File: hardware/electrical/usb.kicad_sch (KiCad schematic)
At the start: 0 parts

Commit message: Add USB PHY IC
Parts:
- added C29, C36, C37: 4u7, symbol Device:C_Small
- added C31, C32, C33, C34, C35: 100n, symbol Device:C_Small
- added C?: DNP, Capacitor_SMD:C_0402_1005Metric, symbol Device:C
- added D3: SMF6.0CA, symbol Device:D_TVS
- added FB?: 0R, Diode_SMD:D_0201_0603Metric, symbol Device:FerriteBead_Small
- added J1: USB_B_Micro, symbol Connector:USB_B_Micro
- added R10: 0R, symbol Device:R
- added R11: 12k±1%, symbol Device:R
- added U6: USB3300-EZK, Package_DFN_QFN:QFN-32-1EP_5x5mm_P0.5mm_EP3.45x3.45mm, symbol Interface_USB:USB3300-EZK
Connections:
- new net: C?.1, D3.2 (A2), FB?.1, J1.1 (VBUS)
- new net: C36.1, U6.29 (VDDA1.8)
- new net: R10.2, U6.4 (VBUS)
- new net: C37.1, U6.15 (VDD1.8), U6.26 (VDD1.8)
- new net: R11.1, U6.32 (RBIAS)
- new net +3V3: C29.1, C31.1, C32.1, C33.1, C34.1, C35.1, U6.16 (VDD3.3), U6.25 (VDD3.3), U6.30 (VDD3.3), U6.31 (REG_EN), U6.6 (VDD3.3)
- new net GND: C29.2, C31.2, C32.2, C33.2, C34.2, C35.2, C36.2, C37.2, C?.2, D3.1 (A1), J1.5 (GND), R11.2, U6.1 (GND), U6.2 (GND), U6.33 (GND)
- new net RCC_MCO_1: U6.28 (XI)
- new net USB_D+: J1.3 (D+), U6.7 (DP)
- new net USB_D-: J1.2 (D-), U6.8 (DM)
- new net USB_OTG_HS_RESET: U6.9 (RESET)
- new net USB_OTG_HS_ULPI_CLK: U6.14 (CLKOUT)
- new net USB_OTG_HS_ULPI_D0: U6.24 (DATA0)
- new net USB_OTG_HS_ULPI_D1: U6.23 (DATA1)
- new net USB_OTG_HS_ULPI_D2: U6.22 (DATA2)
- new net USB_OTG_HS_ULPI_D3: U6.21 (DATA3)
- new net USB_OTG_HS_ULPI_D4: U6.20 (DATA4)
- new net USB_OTG_HS_ULPI_D5: U6.19 (DATA5)
- new net USB_OTG_HS_ULPI_D6: U6.18 (DATA6)
- new net USB_OTG_HS_ULPI_D7: U6.17 (DATA7)
- new net USB_OTG_HS_ULPI_DIR: U6.12 (DIR)
- new net USB_OTG_HS_ULPI_NXT: U6.11 (NXT)
- new net USB_OTG_HS_ULPI_STP: U6.13 (STP)
- new net VBUS: FB?.2, R10.1
- no-connect marks 0 -> 6
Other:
- note added: "C30, C36 and C37 should all be low ESR (<1 Ohm)."
- note added: "NOTES"
- note added: "USB D- and D+ should be routed as a differential pair."
- note added: "USB3300 contains internal ESD protection."
- note added: "VBUS pin must never exceed 5.5V. D3 ensures voltage never exceeds 6V. R10 is available if necessary."
- company: (none) -> Frank Plowman
- title: (none) -> USB

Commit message: Update STM32CubeMX configuration to match schematic and fix ERC
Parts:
- gave numbers to parts that had none: 2
- renumbered C29 to C2, C31 to C3, C32 to C4, C33 to C5, C34 to C6, C35 to C7, C36 to C8, C37 to C9, D3 to D1, R10 to R1, R11 to R2, U6 to U1

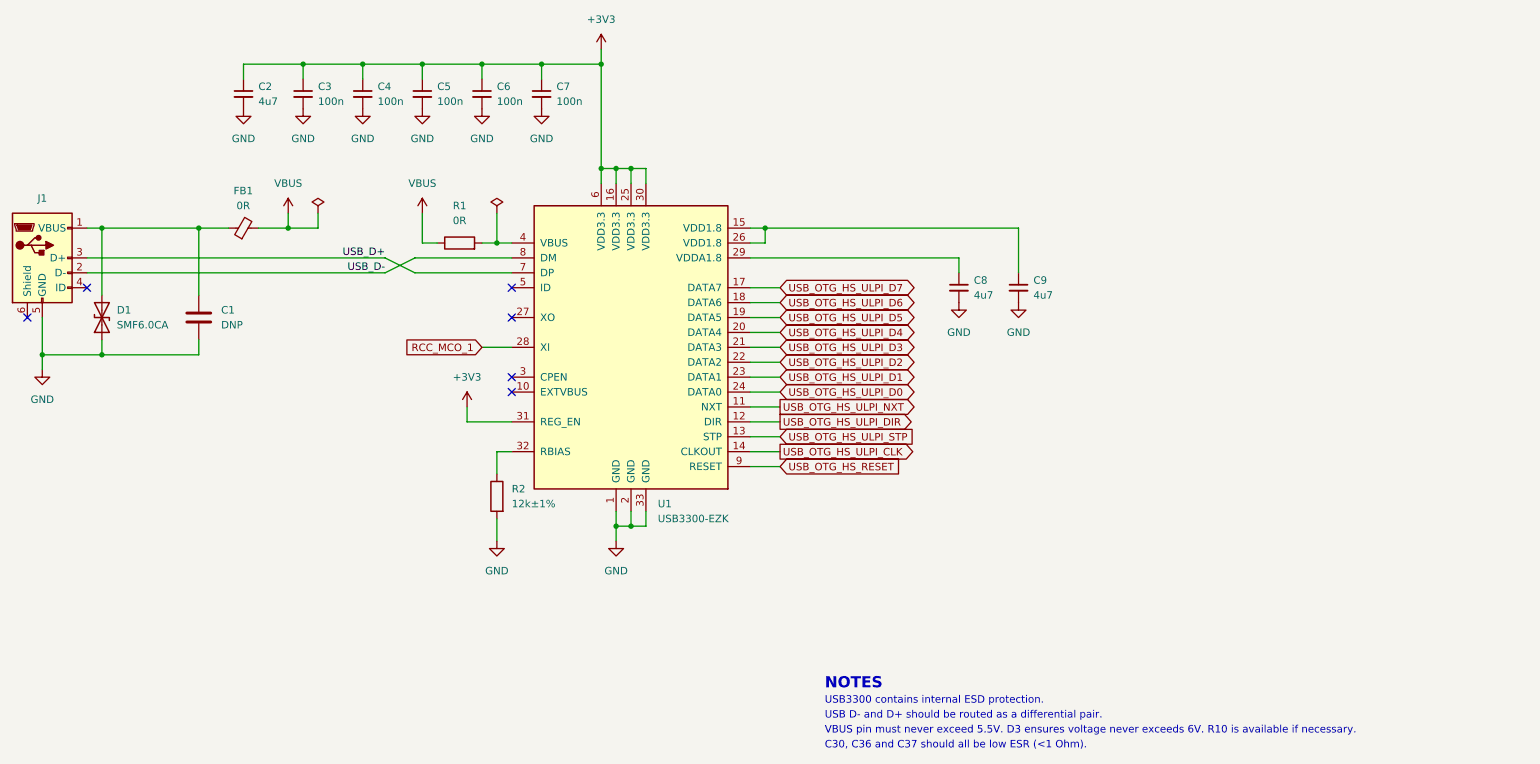
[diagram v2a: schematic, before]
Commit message: USB signal integrity tweaks. * Replace DNP capacitor at USB with 4.7µF per USB specification * Replace 0R ferrite bead with 100Ω@100MHz * Connect shield to ground * Replace 0R VBUS sense resistor with 670Ω to reject spikes 5.5V<V<6V * Add source terminator resistor for clock output
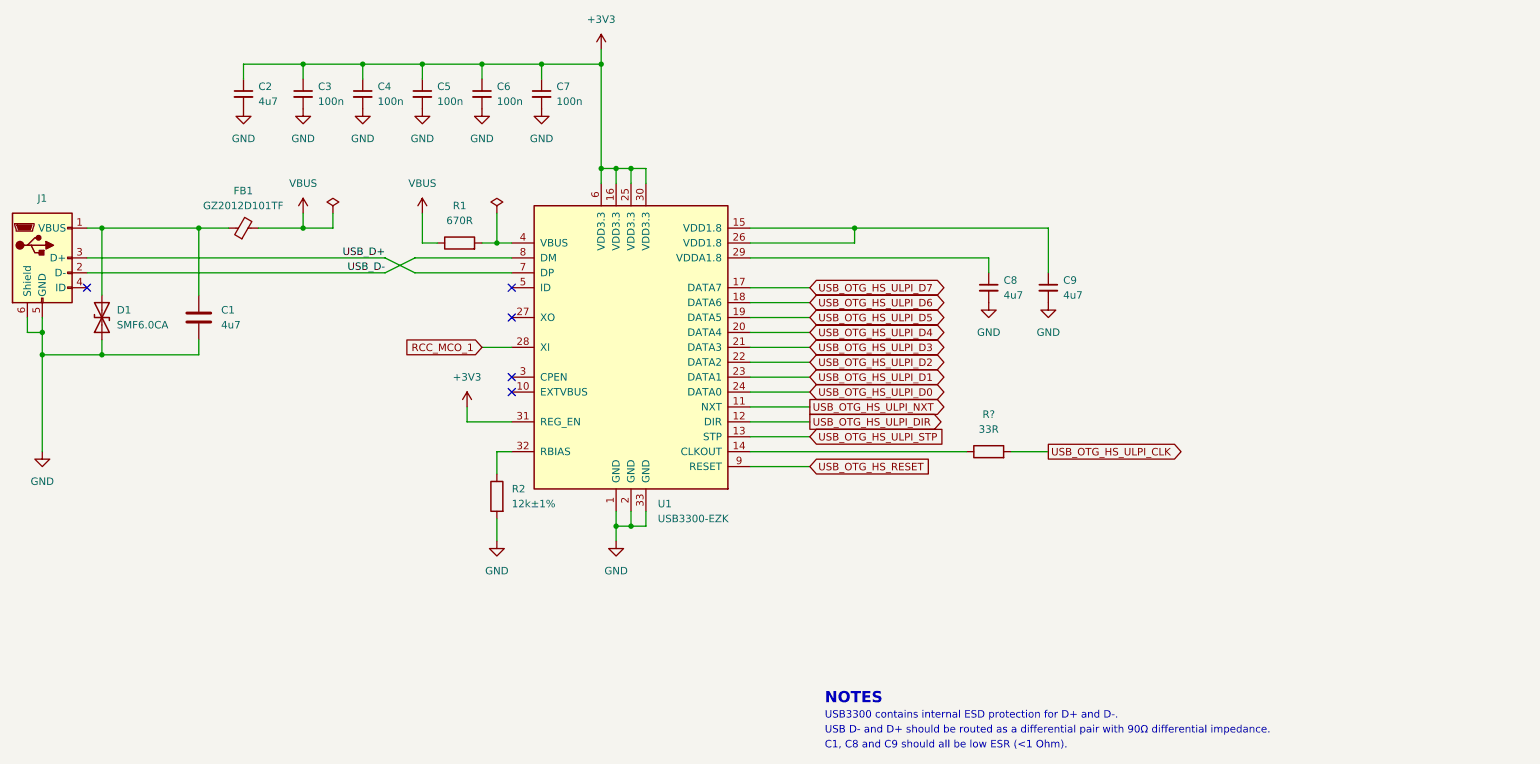
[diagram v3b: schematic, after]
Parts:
- added R?: 33R, symbol Device:R
- C1: value DNP -> 4u7
- FB1: value 0R -> GZ2012D101TF
- R1: value 0R -> 670R
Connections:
- net GND: now also J1.6 (Shield)
- net USB_OTG_HS_ULPI_CLK: now also R?.2; no longer U1.14 (CLKOUT)
- new net: R?.1, U1.14 (CLKOUT)
- no-connect marks 6 -> 5
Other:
- note added: "C1, C8 and C9 should all be low ESR (<1 Ohm)."
- note added: "USB D- and D+ should be routed as a differential pair with 90Ω differential impedance."
- note added: "USB3300 contains internal ESD protection for D+ and D-."
- note removed: "C30, C36 and C37 should all be low ESR (<1 Ohm)."
- note removed: "USB D- and D+ should be routed as a differential pair."
- note removed: "USB3300 contains internal ESD protection."
- note removed: "VBUS pin must never exceed 5.5V. D3 ensures voltage never exceeds 6V. R10 is available if necessary."
- moved on the sheet: C8, C9

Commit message: Minor USB schematic tweaks * Remove extra 100nF decoupling capacitor * Add notes on routing ULPI traces * Schematic formatting tweaks
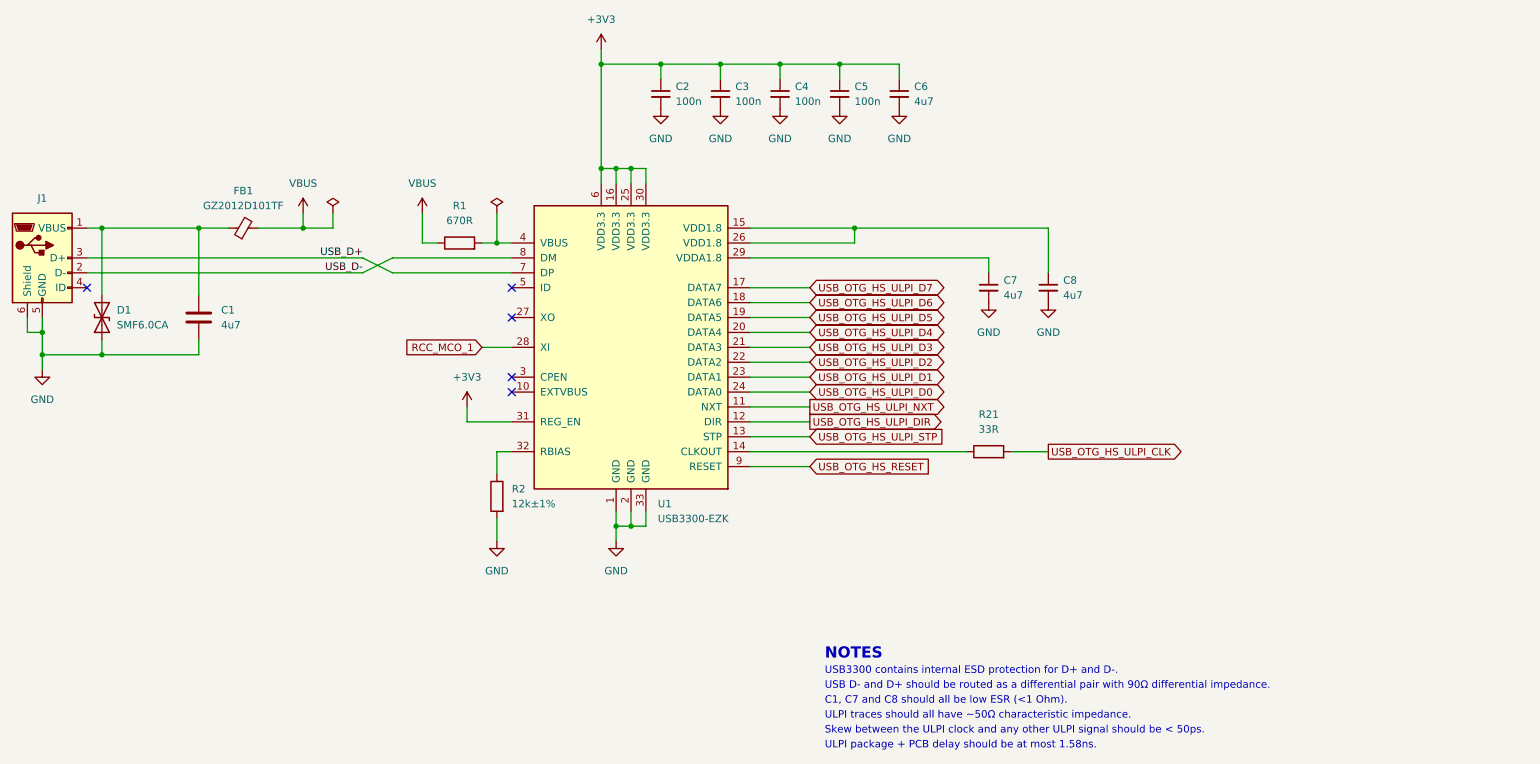
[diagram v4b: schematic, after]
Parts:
- removed C3: 100n, symbol Device:C_Small
- gave numbers to parts that had none: 1
- renumbered C7 to C2, C6 to C3, C5 to C4, C4 to C5, C2 to C6, C8 to C7, C9 to C8
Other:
- note added: "C1, C7 and C8 should all be low ESR (<1 Ohm)."
- note added: "Skew between the ULPI clock and any other ULPI signal should be < 50ps."
- note added: "ULPI package + PCB delay should be at most 1.58ns."
- note added: "ULPI traces should all have ~50Ω characteristic impedance."
- note removed: "C1, C8 and C9 should all be low ESR (<1 Ohm)."
- moved on the sheet: C2, C3, C4, C5, C6

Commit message: Fix schematic formatting (#6)
* Fix schematic formatting

* Clear and re-annotate to fix ERC
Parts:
- renumbered R21 to R3
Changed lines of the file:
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@@
   (symbol (lib_id "power:PWR_FLAG") (at 121.92 73.66 0) (unit 1)
     (in_bom yes) (on_board yes) (fields_autoplaced)
-    (property "Reference" "#FLG01" (id 0) (at 121.92 71.755 0)
+    (property "Reference" "#FLG02" (id 0) (at 121.92 71.755 0)
       (effects (font (size 1.27 1.27)) hide)
     )
@@
   (symbol (lib_id "power:+3V3") (at 139.7 45.72 0) (unit 1)
     (in_bom yes) (on_board yes) (fields_autoplaced)
-    (property "Reference" "#PWR012" (id 0) (at 139.7 49.53 0)
+    (property "Reference" "#PWR06" (id 0) (at 139.7 49.53 0)
       (effects (font (size 1.27 1.27)) hide)
     )
@@
   (symbol (lib_id "power:GND") (at 149.86 55.88 0) (mirror y) (unit 1)
     (in_bom yes) (on_board yes) (fields_autoplaced)
-    (property "Reference" "#PWR011" (id 0) (at 149.86 62.23 0)
+    (property "Reference" "#PWR08" (id 0) (at 149.86 62.23 0)
       (effects (font (size 1.27 1.27)) hide)
     )
@@
   (symbol (lib_id "power:GND") (at 121.92 129.54 0) (unit 1)
     (in_bom yes) (on_board yes) (fields_autoplaced)
-    (property "Reference" "#PWR010" (id 0) (at 121.92 135.89 0)
+    (property "Reference" "#PWR05" (id 0) (at 121.92 135.89 0)
       (effects (font (size 1.27 1.27)) hide)
     )
@@
   (symbol (lib_id "power:PWR_FLAG") (at 93.98 73.66 0) (unit 1)
     (in_bom yes) (on_board yes) (fields_autoplaced)
-    (property "Reference" "#FLG0101" (id 0) (at 93.98 71.755 0)
+    (property "Reference" "#FLG01" (id 0) (at 93.98 71.755 0)
       (effects (font (size 1.27 1.27)) hide)
     )
@@
   (symbol (lib_id "power:+3V3") (at 116.84 106.68 0) (unit 1)
     (in_bom yes) (on_board yes) (fields_autoplaced)
-    (property "Reference" "#PWR08" (id 0) (at 116.84 110.49 0)
+    (property "Reference" "#PWR04" (id 0) (at 116.84 110.49 0)
       (effects (font (size 1.27 1.27)) hide)
     )
@@
   (symbol (lib_id "power:GND") (at 142.24 129.54 0) (unit 1)
     (in_bom yes) (on_board yes) (fields_autoplaced)
-    (property "Reference" "#PWR013" (id 0) (at 142.24 135.89 0)
+    (property "Reference" "#PWR07" (id 0) (at 142.24 135.89 0)
       (effects (font (size 1.27 1.27)) hide)
     )
@@
   (symbol (lib_id "power:GND") (at 180.34 55.88 0) (mirror y) (unit 1)
     (in_bom yes) (on_board yes) (fields_autoplaced)
-    (property "Reference" "#PWR05" (id 0) (at 180.34 62.23 0)
+    (property "Reference" "#PWR011" (id 0) (at 180.34 62.23 0)
       (effects (font (size 1.27 1.27)) hide)
     )
@@
   (symbol (lib_id "power:GND") (at 190.5 55.88 0) (mirror y) (unit 1)
     (in_bom yes) (on_board yes) (fields_autoplaced)
-    (property "Reference" "#PWR02" (id 0) (at 190.5 62.23 0)
+    (property "Reference" "#PWR012" (id 0) (at 190.5 62.23 0)
       (effects (font (size 1.27 1.27)) hide)
     )
@@
   (symbol (lib_id "power:VBUS") (at 109.22 73.66 0) (unit 1)
     (in_bom yes) (on_board yes) (fields_autoplaced)
-    (property "Reference" "#PWR07" (id 0) (at 109.22 77.47 0)
+    (property "Reference" "#PWR03" (id 0) (at 109.22 77.47 0)
       (effects (font (size 1.27 1.27)) hide)
     )
@@
   (symbol (lib_id "power:GND") (at 170.18 55.88 0) (mirror y) (unit 1)
     (in_bom yes) (on_board yes) (fields_autoplaced)
-    (property "Reference" "#PWR06" (id 0) (at 170.18 62.23 0)
+    (property "Reference" "#PWR010" (id 0) (at 170.18 62.23 0)
       (effects (font (size 1.27 1.27)) hide)
     )
@@
   (symbol (lib_id "power:GND") (at 205.74 88.9 0) (unit 1)
     (in_bom yes) (on_board yes) (fields_autoplaced)
-    (property "Reference" "#PWR014" (id 0) (at 205.74 95.25 0)
+    (property "Reference" "#PWR013" (id 0) (at 205.74 95.25 0)
       (effects (font (size 1.27 1.27)) hide)
     )
@@
   (symbol (lib_id "Device:R") (at 205.74 114.3 90) (unit 1)
     (in_bom yes) (on_board yes) (fields_autoplaced)
-    (property "Reference" "R21" (id 0) (at 205.74 107.95 90))
+    (property "Reference" "R3" (id 0) (at 205.74 107.95 90))
     (property "Value" "33R" (id 1) (at 205.74 110.49 90))
     (property "Footprint" "" (id 2) (at 205.74 116.078 90)
@@
   (symbol (lib_id "power:VBUS") (at 88.9 73.66 0) (unit 1)
     (in_bom yes) (on_board yes) (fields_autoplaced)
-    (property "Reference" "#PWR03" (id 0) (at 88.9 77.47 0)
+    (property "Reference" "#PWR02" (id 0) (at 88.9 77.47 0)
       (effects (font (size 1.27 1.27)) hide)
     )
@@
   (symbol (lib_id "power:GND") (at 215.9 88.9 0) (unit 1)
     (in_bom yes) (on_board yes) (fields_autoplaced)
-    (property "Reference" "#PWR015" (id 0) (at 215.9 95.25 0)
-      (effects (font (size 1.27 1.27)) hide)
-    )
+    (property "Reference" "#PWR014" (id 0) (at 215.9 95.25 0)
+      (effects (font (size 1.27 1.27)) hide)
+    )

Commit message: Update footprints to KiCad 7.0 versions
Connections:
- net at C8.1, U1.15 (VDD1.8): no longer U1.26 (VDD1.8)
- no-connect marks 5 -> 6
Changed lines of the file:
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@@
   (junction (at 180.34 48.26) (diameter 0) (color 0 0 0 0)
-  )
-  (junction (at 182.88 76.2) (diameter 0) (color 0 0 0 0)
   )
   (junction (at 144.78 66.04) (diameter 0) (color 0 0 0 0)
@@
   (no_connect (at 52.07 86.36))
   (no_connect (at 124.46 91.44))
+  (no_connect (at 165.1 78.74))
   (wire (pts (xy 121.92 73.66) (xy 121.92 78.74))
     (stroke (width 0) (type default))
@@
     (stroke (width 0) (type default))
   )
-  (wire (pts (xy 182.88 78.74) (xy 182.88 76.2))
-    (stroke (width 0) (type default))
-  )
   (wire (pts (xy 71.12 76.2) (xy 71.12 87.63))
     (stroke (width 0) (type default))
@@
     (stroke (width 0) (type default))
   )
-  (wire (pts (xy 182.88 76.2) (xy 215.9 76.2))
+  (wire (pts (xy 165.1 76.2) (xy 215.9 76.2))
     (stroke (width 0) (type default))
   )
@@
     (stroke (width 0) (type default))
   )
-  (wire (pts (xy 165.1 76.2) (xy 182.88 76.2))
-    (stroke (width 0) (type default))
-  )
   (wire (pts (xy 41.91 93.98) (xy 44.45 93.98))
     (stroke (width 0) (type default))
@@
     (stroke (width 0) (type default))
   )
-  (wire (pts (xy 165.1 78.74) (xy 182.88 78.74))
-    (stroke (width 0) (type default))
-  )

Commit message: Use VDD in place of +3.3V more extensively
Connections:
- net +3V3: no longer C2.1, C3.1, C4.1, C5.1, C6.1, U1.16 (VDD3.3), U1.25 (VDD3.3), U1.30 (VDD3.3), U1.6 (VDD3.3)
- new net VDD: C2.1, C3.1, C4.1, C5.1, C6.1, U1.16 (VDD3.3), U1.25 (VDD3.3), U1.30 (VDD3.3), U1.6 (VDD3.3)
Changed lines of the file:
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@@
-    )
-  )
-  (symbol (lib_id "power:+3V3") (at 139.7 45.72 0) (unit 1)
-    (in_bom yes) (on_board yes) (dnp no) (fields_autoplaced)
-    (property "Reference" "#PWR06" (at 139.7 49.53 0)
-      (effects (font (size 1.27 1.27)) hide)
-    )
-    (property "Value" "+3V3" (at 139.7 40.64 0)
-      (effects (font (size 1.27 1.27)))
-    )
-    (property "Footprint" "" (at 139.7 45.72 0)
-      (effects (font (size 1.27 1.27)) hide)
-    )
-    (property "Datasheet" "" (at 139.7 45.72 0)
-      (effects (font (size 1.27 1.27)) hide)
-    )
-    (pin "1")
-    (instances
-      (project "3885"
-        (path "/7363a4f0-2da1-4086-abed-ea6709c3a185/b2a90f2c-c4bd-40df-ad3c-0b37c5fa6b32"
-          (reference "#PWR06") (unit 1)
-        )
-      )
     )
   )
@@
         )
       )
+    )
+  )
+  (symbol (lib_id "power:VDD") (at 139.7 45.72 0) (unit 1)
+    (in_bom yes) (on_board yes) (dnp no) (fields_autoplaced)
+    (property "Reference" "#PWR06" (at 139.7 49.53 0)
+      (effects (font (size 1.27 1.27)) hide)
+    )
+    (property "Value" "VDD" (at 139.7 41.91 0)
+      (effects (font (size 1.27 1.27)))
+    )
+    (property "Footprint" "" (at 139.7 45.72 0)
+      (effects (font (size 1.27 1.27)) hide)
+    )
+    (property "Datasheet" "" (at 139.7 45.72 0)
+      (effects (font (size 1.27 1.27)) hide)
+    )
+    (pin "1")
+    (instances
+      (project "3885"
+        (path "/7363a4f0-2da1-4086-abed-ea6709c3a185/b2a90f2c-c4bd-40df-ad3c-0b37c5fa6b32"
+          (reference "#PWR06") (unit 1)
+        )
+      )
